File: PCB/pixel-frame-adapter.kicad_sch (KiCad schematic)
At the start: 4 parts, among them U2 Adafruit_ItsyBitsy_M4, U3 Adafruit_LIS3DH

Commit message: routing done
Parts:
- removed R1: 0, Resistor_SMD:R_0603_1608Metric_Pad0.98x0.95mm_HandSolder, symbol Device:R
- added JP1: (no value), symbol Jumper:SolderJumper_2_Bridged
- U1: value (none) -> Adafruit_1_54in_TFT; footprint (none) -> Display:Adafruit_2_54in_TFT_Display
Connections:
- net BACKLIGHT: now also JP1.1 (A)
- net at U1.11 (BL): now also JP1.2 (B)
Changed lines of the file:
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@@
       (effects (font (size 1.27 1.27)) (justify left))
     )
-    (property "Value" "" (id 1) (at 153.67 78.74 0)
+    (property "Value" "Adafruit_1_54in_TFT" (id 1) (at 153.67 78.74 0)
       (effects (font (size 1.27 1.27)) (justify left))
     )
-    (property "Footprint" "" (id 2) (at 154.94 114.3 0)
+    (property "Footprint" "Display:Adafruit_2_54in_TFT_Display" (id 2) (at 154.94 114.3 0)
       (effects (font (size 1.27 1.27)) hide)
     )
@@
     (pin "1")
   )
-  (symbol (lib_id "Device:R") (at 146.05 107.95 90) (unit 1)
-    (in_bom yes) (on_board yes)
-    (property "Reference" "R1" (id 0) (at 147.32 110.49 90))
-    (property "Value" "0" (id 1) (at 144.78 110.49 90))
-    (property "Footprint" "Resistor_SMD:R_0603_1608Metric_Pad0.98x0.95mm_HandSolder" (id 2) (at 146.05 109.728 90)
-      (effects (font (size 1.27 1.27)) hide)
-    )
-    (property "Datasheet" "~" (id 3) (at 146.05 107.95 0)
-      (effects (font (size 1.27 1.27)) hide)
-    )
-    (pin "1")
-    (pin "2")
-  )
   (symbol (lib_id "power:GND") (at 109.22 95.25 0) (unit 1)
     (in_bom yes) (on_board yes) (fields_autoplaced)
@@
     )
     (pin "1")
+  )
+  (symbol (lib_id "Jumper:SolderJumper_2_Bridged") (at 146.05 107.95 0) (unit 1)
+    (in_bom yes) (on_board yes)
+    (property "Reference" "JP1" (id 0) (at 146.05 110.49 0))
+    (property "Value" "" (id 1) (at 137.16 111.76 0)
+      (effects (font (size 1.27 1.27)) hide)
+    )
+    (property "Footprint" "" (id 2) (at 146.05 107.95 0)
+      (effects (font (size 1.27 1.27)) hide)
+    )
+    (property "Datasheet" "~" (id 3) (at 146.05 107.95 0)
+      (effects (font (size 1.27 1.27)) hide)
+    )
+    (pin "1")
+    (pin "2")
   )
   (sheet_instances
@@
       (reference "#PWR06") (unit 1) (value "+5V") (footprint "")
     )
-    (path "/d7c6adaa-9eba-46a5-ad4c-ebb3131203f3"
-      (reference "R1") (unit 1) (value "0") (footprint "Resistor_SMD:R_0603_1608Metric_Pad0.98x0.95mm_HandSolder")
+    (path "/eb8e38cd-dc17-4593-889c-e9f58005f6e7"
+      (reference "JP1") (unit 1) (value "SolderJumper_2_Bridged") (footprint "Jumper:SolderJumper-2_P1.3mm_Bridged_RoundedPad1.0x1.5mm")
     )
     (path "/b4c36a25-2699-411b-86a4-19027d125910"

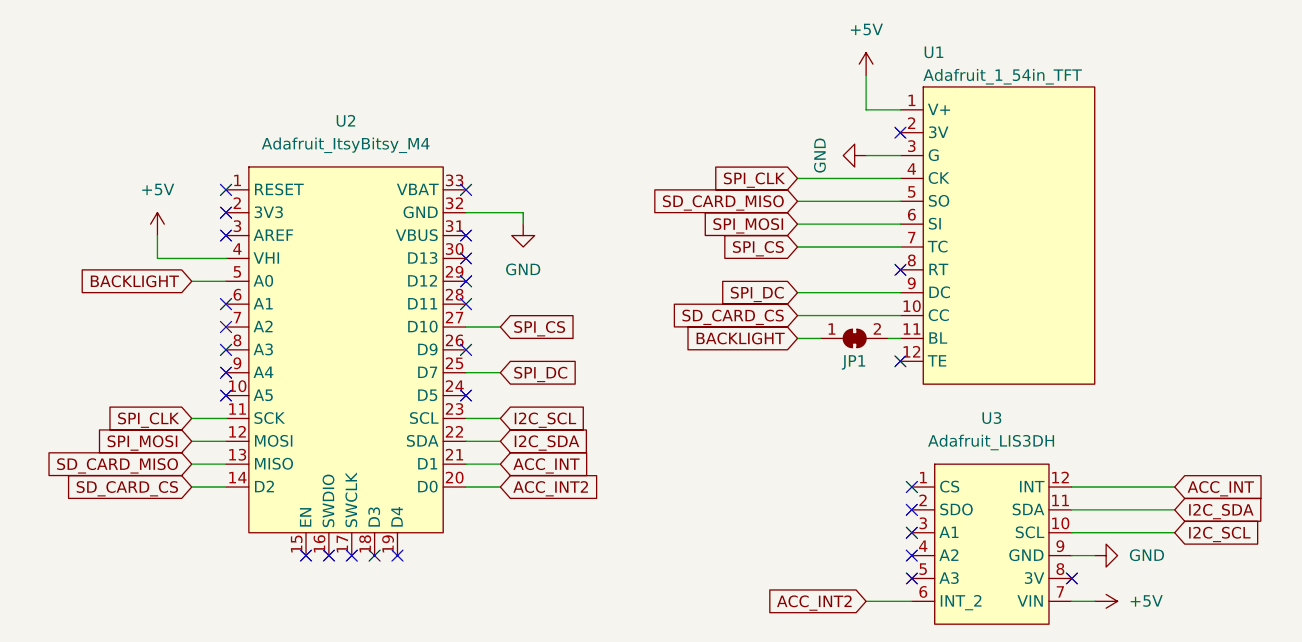
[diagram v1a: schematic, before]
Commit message: dimensions and track cleanup
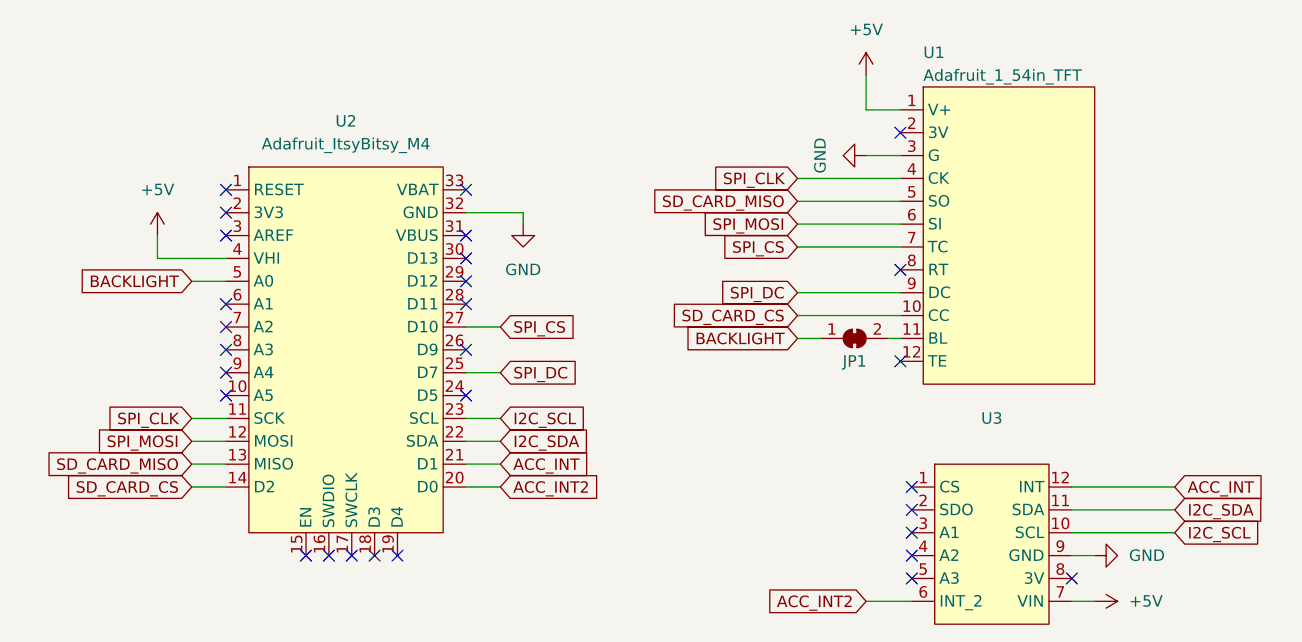
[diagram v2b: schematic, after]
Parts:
- JP1: value (none) -> SolderJumper_2_Bridged; footprint (none) -> pixel-frame-library:SolderJumper-2_P1.3mm_Bridged_RoundedPad1.0x1.5mm
- U1: footprint Display:Adafruit_2_54in_TFT_Display -> pixel-frame-library:Adafruit_2_54in_TFT_Display
- U2: footprint Module:Adafruit_ItsyBitsy_M4 -> pixel-frame-library:Adafruit_ItsyBitsy_M4
- U3: value Adafruit_LIS3DH -> (none); footprint Sensor_Motion:Adafruit_LIS3DH -> (none)
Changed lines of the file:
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@@
     )
   )
-  (symbol (lib_id "MCU_Module:Adafruit_ItsyBitsy_M4") (at 85.09 87.63 0) (unit 1)
+  (symbol (lib_id "MCU_Module:Adafruit_ItsyBitsy_M4") (at 88.9 106.68 0) (unit 1)
     (in_bom yes) (on_board yes) (fields_autoplaced)
     (property "Reference" "U2" (id 0) (at 89.535 83.82 0))
     (property "Value" "Adafruit_ItsyBitsy_M4" (id 1) (at 89.535 86.36 0))
-    (property "Footprint" "Module:Adafruit_ItsyBitsy_M4" (id 2) (at 80.01 130.81 0)
+    (property "Footprint" "pixel-frame-library:Adafruit_ItsyBitsy_M4" (id 2) (at 88.9 138.43 0)
       (effects (font (size 1.27 1.27)) hide)
     )
@@
     (in_bom yes) (on_board yes) (fields_autoplaced)
     (property "Reference" "U3" (id 0) (at 161.29 116.84 0))
-    (property "Value" "Adafruit_LIS3DH" (id 1) (at 161.29 119.38 0))
-    (property "Footprint" "Sensor_Motion:Adafruit_LIS3DH" (id 2) (at 161.29 125.73 0)
+    (property "Value" "" (id 1) (at 161.29 119.38 0))
+    (property "Footprint" "" (id 2) (at 161.29 125.73 0)
       (effects (font (size 1.27 1.27)) hide)
     )
@@
     (pin "1")
   )
-  (symbol (lib_id "Display_Graphic:Adafruit_1_54in_TFT") (at 160.02 74.93 0) (unit 1)
+  (symbol (lib_id "Display_Graphic:Adafruit_1_54in_TFT") (at 162.56 96.52 0) (unit 1)
     (in_bom yes) (on_board yes)
     (property "Reference" "U1" (id 0) (at 153.67 76.2 0)
@@
       (effects (font (size 1.27 1.27)) (justify left))
     )
-    (property "Footprint" "Display:Adafruit_2_54in_TFT_Display" (id 2) (at 154.94 114.3 0)
+    (property "Footprint" "pixel-frame-library:Adafruit_2_54in_TFT_Display" (id 2) (at 163.83 114.3 0)
       (effects (font (size 1.27 1.27)) hide)
     )
@@
     (in_bom yes) (on_board yes)
     (property "Reference" "JP1" (id 0) (at 146.05 110.49 0))
-    (property "Value" "" (id 1) (at 137.16 111.76 0)
-      (effects (font (size 1.27 1.27)) hide)
-    )
-    (property "Footprint" "" (id 2) (at 146.05 107.95 0)
+    (property "Value" "SolderJumper_2_Bridged" (id 1) (at 146.05 113.03 0)
+      (effects (font (size 1.27 1.27)) hide)
+    )
+    (property "Footprint" "pixel-frame-library:SolderJumper-2_P1.3mm_Bridged_RoundedPad1.0x1.5mm" (id 2) (at 146.05 105.41 0)
       (effects (font (size 1.27 1.27)) hide)
     )
@@
     )
     (path "/eb8e38cd-dc17-4593-889c-e9f58005f6e7"
-      (reference "JP1") (unit 1) (value "SolderJumper_2_Bridged") (footprint "Jumper:SolderJumper-2_P1.3mm_Bridged_RoundedPad1.0x1.5mm")
+      (reference "JP1") (unit 1) (value "SolderJumper_2_Bridged") (footprint "pixel-frame-library:SolderJumper-2_P1.3mm_Bridged_RoundedPad1.0x1.5mm")
     )
     (path "/b4c36a25-2699-411b-86a4-19027d125910"
-      (reference "U1") (unit 1) (value "Adafruit_1_54in_TFT") (footprint "Display:Adafruit_2_54in_TFT_Display")
+      (reference "U1") (unit 1) (value "Adafruit_1_54in_TFT") (footprint "pixel-frame-library:Adafruit_2_54in_TFT_Display")
     )
     (path "/06fb08fe-6221-4517-8c13-6e804e6adc4b"
-      (reference "U2") (unit 1) (value "Adafruit_ItsyBitsy_M4") (footprint "Module:Adafruit_ItsyBitsy_M4")
+      (reference "U2") (unit 1) (value "Adafruit_ItsyBitsy_M4") (footprint "pixel-frame-library:Adafruit_ItsyBitsy_M4")
     )
     (path "/564131df-3b09-4b0e-bf8a-31d122a6d3be"
-      (reference "U3") (unit 1) (value "Adafruit_LIS3DH") (footprint "Sensor_Motion:Adafruit_LIS3DH")
-    )
-  )
+      (reference "U3") (unit 1) (value "Adafruit_LIS3DH") (footprint "pixel-frame-library:Adafruit_LIS3DH")
+    )
+  )

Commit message: clean up
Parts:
- U3: value (none) -> Adafruit_LIS3DH; footprint (none) -> pixel-frame-library:Adafruit_LIS3DH
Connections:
- net RST: now reaches U2.30 (D13)
- net RST: now also U1.8 (RT)
- no-connect marks 29 -> 27
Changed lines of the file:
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@@
   (paper "A4")
   (no_connect (at 151.13 110.49))
-  (no_connect (at 151.13 100.33))
   (no_connect (at 151.13 85.09))
   (no_connect (at 170.18 134.62))
@@
   (no_connect (at 152.4 129.54))
   (no_connect (at 102.87 91.44))
-  (no_connect (at 102.87 99.06))
   (no_connect (at 102.87 96.52))
   (no_connect (at 102.87 104.14))
@@
     (stroke (width 0) (type default) (color 0 0 0 0))
   )
+  (wire (pts (xy 139.7 100.33) (xy 151.13 100.33))
+    (stroke (width 0) (type default) (color 0 0 0 0))
+  )
   (wire (pts (xy 72.39 116.84) (xy 76.2 116.84))
     (stroke (width 0) (type default) (color 0 0 0 0))
@@
     (stroke (width 0) (type default) (color 0 0 0 0))
   )
+  (wire (pts (xy 102.87 93.98) (xy 106.68 93.98))
+    (stroke (width 0) (type default) (color 0 0 0 0))
+  )
   (wire (pts (xy 139.7 95.25) (xy 151.13 95.25))
     (stroke (width 0) (type default) (color 0 0 0 0))
   )
-  (wire (pts (xy 109.22 93.98) (xy 109.22 95.25))
-    (stroke (width 0) (type default) (color 0 0 0 0))
-  )
   (wire (pts (xy 102.87 121.92) (xy 106.68 121.92))
     (stroke (width 0) (type default) (color 0 0 0 0))
@@
     (stroke (width 0) (type default) (color 0 0 0 0))
   )
-  (wire (pts (xy 102.87 93.98) (xy 109.22 93.98))
-    (stroke (width 0) (type default) (color 0 0 0 0))
-  )
   (wire (pts (xy 72.39 119.38) (xy 76.2 119.38))
     (stroke (width 0) (type default) (color 0 0 0 0))
@@
     (stroke (width 0) (type default) (color 0 0 0 0))
   )
+  (wire (pts (xy 102.87 99.06) (xy 106.68 99.06))
+    (stroke (width 0) (type default) (color 0 0 0 0))
+  )
   (wire (pts (xy 170.18 129.54) (xy 181.61 129.54))
     (stroke (width 0) (type default) (color 0 0 0 0))
@@
     )
   )
+  (global_label "RST" (shape input) (at 139.7 100.33 180) (fields_autoplaced)
+    (effects (font (size 1.27 1.27)) (justify right))
+    (property "Intersheet References" "${INTERSHEET_REFS}" (id 0) (at 133.8398 100.2506 0)
+      (effects (font (size 1.27 1.27)) (justify right) hide)
+    )
+  )
   (global_label "SD_CARD_CS" (shape input) (at 72.39 124.46 180) (fields_autoplaced)
     (effects (font (size 1.27 1.27)) (justify right))
     (property "Intersheet References" "${INTERSHEET_REFS}" (id 0) (at 58.184 124.3806 0)
       (effects (font (size 1.27 1.27)) (justify right) hide)
+    )
+  )
+  (global_label "RST" (shape input) (at 106.68 99.06 0) (fields_autoplaced)
+    (effects (font (size 1.27 1.27)) (justify left))
+    (property "Intersheet References" "${INTERSHEET_REFS}" (id 0) (at 112.5402 99.1394 0)
+      (effects (font (size 1.27 1.27)) (justify left) hide)
     )
   )
@@
     (in_bom yes) (on_board yes) (fields_autoplaced)
     (property "Reference" "U3" (id 0) (at 161.29 116.84 0))
-    (property "Value" "" (id 1) (at 161.29 119.38 0))
-    (property "Footprint" "" (id 2) (at 161.29 125.73 0)
+    (property "Value" "Adafruit_LIS3DH" (id 1) (at 161.29 119.38 0))
+    (property "Footprint" "pixel-frame-library:Adafruit_LIS3DH" (id 2) (at 161.29 125.73 0)
       (effects (font (size 1.27 1.27)) hide)
     )
@@
     (pin "1")
   )
-  (symbol (lib_id "power:GND") (at 109.22 95.25 0) (unit 1)
-    (in_bom yes) (on_board yes) (fields_autoplaced)
-    (property "Reference" "#PWR03" (id 0) (at 109.22 101.6 0)
-      (effects (font (size 1.27 1.27)) hide)
-    )
-    (property "Value" "GND" (id 1) (at 109.22 100.33 0))
-    (property "Footprint" "" (id 2) (at 109.22 95.25 0)
-      (effects (font (size 1.27 1.27)) hide)
-    )
-    (property "Datasheet" "" (id 3) (at 109.22 95.25 0)
-      (effects (font (size 1.27 1.27)) hide)
-    )
+  (symbol (lib_id "power:GND") (at 106.68 93.98 90) (unit 1)
+    (in_bom yes) (on_board yes) (fields_autoplaced)
+    (property "Reference" "#PWR03" (id 0) (at 113.03 93.98 0)
+      (effects (font (size 1.27 1.27)) hide)
+    )
+    (property "Value" "GND" (id 1) (at 110.49 93.9799 90)
+      (effects (font (size 1.27 1.27)) (justify right))
+    )
+    (property "Footprint" "" (id 2) (at 106.68 93.98 0)
+      (effects (font (size 1.27 1.27)) hide)
+    )
+    (property "Datasheet" "" (id 3) (at 106.68 93.98 0)
+      (effects (font (size 1.27 1.27)) hide)
+    )
